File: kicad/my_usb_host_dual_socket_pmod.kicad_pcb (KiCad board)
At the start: 2 copper layers, 38.6 x 17.4 mm, 16 parts, among them J1 USB_A_Stacked, J2 Conn_02x06_Odd_Even, J3 Conn_01x02_Socket, U2 QX2303L50T

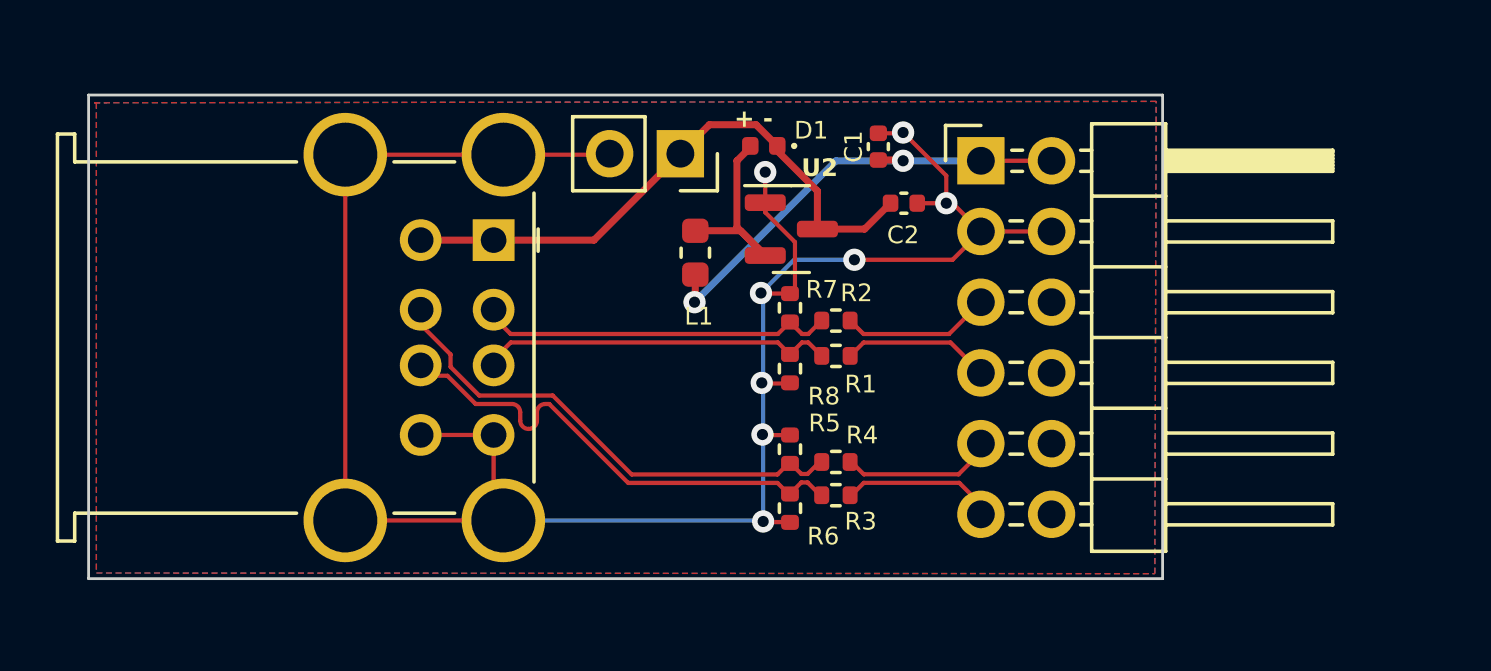
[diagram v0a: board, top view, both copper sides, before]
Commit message: Changed 5V0 regulator to TPS61253A which supports more current
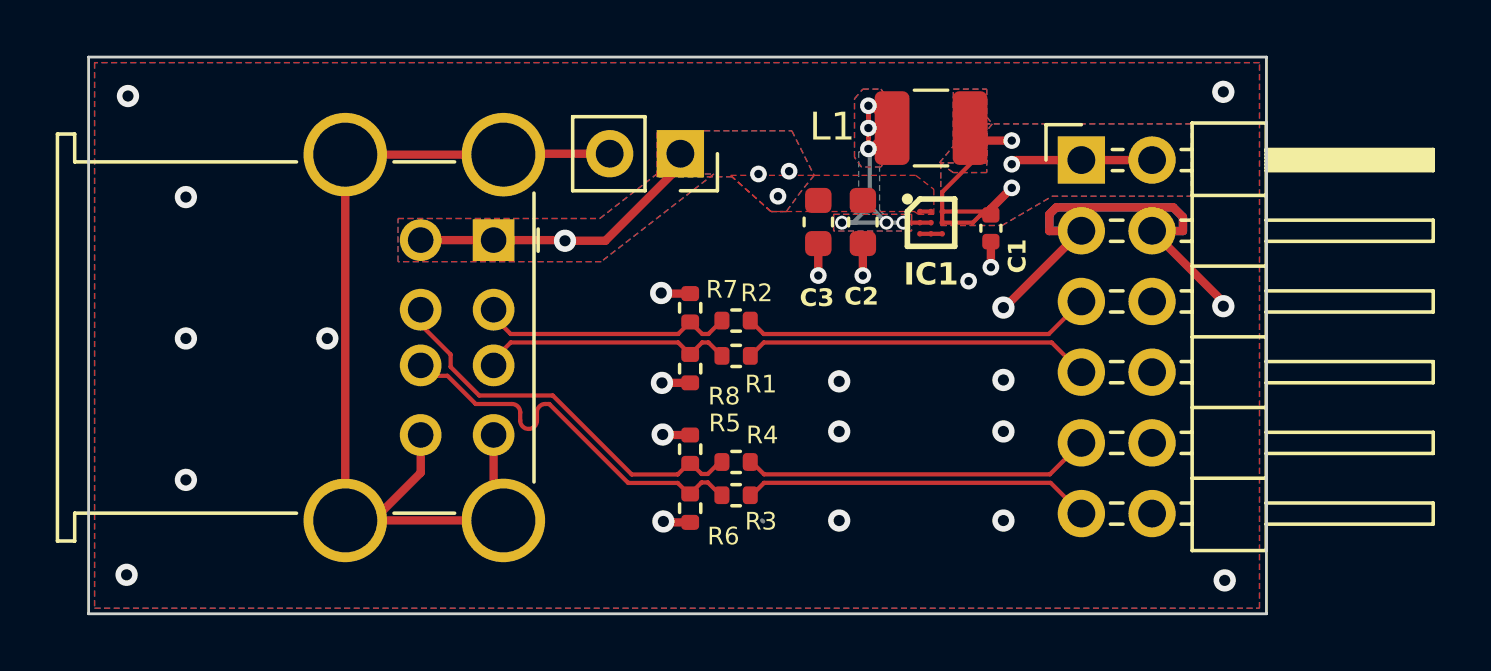
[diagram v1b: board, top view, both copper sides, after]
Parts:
- removed D1: 1N5817/1N5819/1N5822, Diode_SMD:D_0402_1005Metric
- removed U2: QX2303L50T, Package_TO_SOT_SMD:SOT-23
- added C3: 10uF, Capacitor_SMD:C_0603_1608Metric, F.Cu at (98.3, 45.1)
- added IC1: TPS61253AYFFR, libs:BGA9C40P3X3_119X129X62, F.Cu at (102.3, 45.1)
- C2: footprint Capacitor_SMD:C_0402_1005Metric -> Capacitor_SMD:C_0603_1608Metric
- J1: value USB_A_Stacked -> UK-USB AF 90-19.6
- L1: value 10uH -> DFE322512F-1R0M=P2; footprint Inductor_SMD:L_0603_1608Metric -> Inductor_SMD:L_1210_3225Metric
- moved L1 9.58 mm to (102.3, 41.8), turned to 180 degrees
- moved C1 4.99 mm to (104.5, 45.4), turned to -90 degrees
- moved J2 3.61 mm to (107.8, 42.9)
- moved R1 3.58 mm to (95.3, 49.9)
- moved R2 3.58 mm to (95.3, 48.7)
- moved R3 3.58 mm to (95.3, 54.9)
- moved R4 3.58 mm to (95.3, 53.7)
- moved R5 3.58 mm to (93.7, 53.3)
- moved R6 3.58 mm to (93.7, 55.4)
- moved R7 3.58 mm to (93.7, 48.2)
- moved R8 3.58 mm to (93.7, 50.4)
- moved C2 1.62 mm to (99.9, 45.1), turned to -90 degrees
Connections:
- L1 pad 2: Net-(D1-A) -> /IC1-SW
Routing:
- net /IC1-SW: track 0.00 -> 14.5 mm, vias 0 -> 6
- net GND: track 79.0 -> 67.3 mm, vias 8 -> 24
- net /PWR5V0: track 21.4 -> 10.9 mm, vias 0 -> 4
- net Net-(D1-A): track 7.47 -> 0.00 mm
- net /USB1_DN: track 5.37 -> 12.6 mm
- net /USB1_DP: track 5.35 -> 12.5 mm
- net /USB2_DN: track 5.52 -> 12.5 mm
- net /USB2_DP: track 5.56 -> 12.5 mm
- net /USB2t_DN: track 18.0 -> 13.8 mm
- net /USB2t_DP: track 17.9 -> 13.8 mm
- net /USB1t_DN: track 12.9 -> 9.01 mm
- net /USB1t_DP: track 12.8 -> 9.01 mm
- net /PWR3V3: track 16.8 -> 14.3 mm, vias 2 -> 3
- added copper zone on B.Cu, net /IC1-SW
- added copper zone on F.Cu, net /IC1-SW
- added copper zone on B.Cu, net /PWR3V3
- added copper zone on F.Cu, net /PWR3V3
- added copper zone on B.Cu, net /PWR5V0
- added copper zone on F.Cu, net /PWR5V0
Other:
- board size 38.6 x 17.4 mm -> 42.3 x 20 mm
- board text removed: "+ -"
